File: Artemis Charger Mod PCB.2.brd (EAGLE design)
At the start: 95.9 x 94.6 mm, 159 parts, among them J1 MOLEX_CLICKMATE-2-VERTICAL, J2 MOLEX_CLICKMATE-4-VERTICAL, J3 MOLEX_CLICKMATE-2-VERTICAL, J4 MOLEX_CLICKMATE-2-VERTICAL, J5 MOLEX_CLICKMATE-2-VERTICAL, Q10 BSS138, Q11 BSS138, Q8 BSS138, Q9 BSS138, U10 TPS562219, U11 ISO7340, U12 ISO7340, U13 TPS562219, U14 MCP2515-TSSOP, U15 MCP2562, U17 CD4050BD, U18 CD4043B, U19 SN74LVC08ASOIC, U20 SN74LVC32ASOIC, U22 LTC1155, U23 CSD17506Q5A, U26 CSD17506Q5A, U27 LTC1155, U28 CSD17506Q5A, U29 LTC1155, U3 MAX5812, U30 CSD17506Q5A, U32 CSD17506Q5A, U34 CSD17506Q5A, U49 TL7712A-SOIC, U8 MAX5812, U9 TPS562219

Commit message: Fixed LED Silkscreens
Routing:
- net SI_SPI: track 95.7 -> 106.7 mm
- net SO_SPI: track 92.0 -> 97.7 mm
- net CS_SPI: track 52.6 -> 56.5 mm
- net SCK_SPI: track 103.5 -> 106.1 mm
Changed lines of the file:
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@@
 <wire x1="95.25" y1="-14.605" x2="-0.635" y2="-14.605" width="0" layer="20"/>
 <wire x1="-0.635" y1="-14.605" x2="-0.635" y2="80.01" width="0" layer="20"/>
-<wire x1="63.5" y1="69.85" x2="69.85" y2="69.85" width="0.254" layer="21"/>
-<wire x1="69.85" y1="69.85" x2="69.85" y2="65.405" width="0.254" layer="21"/>
-<wire x1="69.85" y1="65.405" x2="67.945" y2="65.405" width="0.254" layer="21"/>
-<wire x1="67.945" y1="65.405" x2="63.5" y2="65.405" width="0.254" layer="21"/>
-<wire x1="63.5" y1="65.405" x2="63.5" y2="69.85" width="0.254" layer="21"/>
+<wire x1="67.056" y1="70.358" x2="70.866" y2="70.358" width="0.254" layer="21"/>
+<wire x1="70.866" y1="70.358" x2="70.866" y2="65.151" width="0.254" layer="21"/>
+<wire x1="70.866" y1="65.151" x2="67.945" y2="65.151" width="0.254" layer="21"/>
+<wire x1="67.945" y1="65.151" x2="67.056" y2="65.151" width="0.254" layer="21"/>
+<wire x1="67.056" y1="65.151" x2="67.056" y2="70.358" width="0.254" layer="21"/>
 <wire x1="66.04" y1="56.515" x2="66.04" y2="55.88" width="0.254" layer="21"/>
 <wire x1="66.04" y1="55.88" x2="66.04" y2="52.705" width="0.254" layer="21"/>
@@
 <wire x1="66.04" y1="44.45" x2="66.04" y2="52.705" width="0.254" layer="21"/>
 <wire x1="84.455" y1="44.45" x2="66.04" y2="44.45" width="0.254" layer="21"/>
-<wire x1="67.945" y1="65.405" x2="67.945" y2="55.88" width="0.254" layer="21"/>
+<wire x1="67.945" y1="65.151" x2="67.945" y2="55.88" width="0.254" layer="21"/>
 <wire x1="67.945" y1="55.88" x2="66.04" y2="55.88" width="0.254" layer="21"/>
 <text x="40.64" y="-3.175" size="0.762" layer="21">Power Brick</text>
@@
 <attribute name="MF" value="" x="48.26" y="74.93" size="1.778" layer="27" display="off"/>
 <attribute name="PARTNO" value="598-8170-107F" x="48.26" y="74.93" size="1.778" layer="27" display="off"/>
-<attribute name="NAME" x="64.135" y="66.04" size="1.27" layer="25" font="vector"/>
+<attribute name="NAME" x="70.358" y="64.389" size="1.27" layer="25" font="vector" rot="R90"/>
 <attribute name="VALUE" x="67.31" y="53.34" size="1.27" layer="27" rot="R90"/>
 </element>
@@
 <attribute name="MF" value="" x="34.29" y="74.93" size="1.778" layer="27" display="off"/>
 <attribute name="PARTNO" value="598-8170-107F" x="34.29" y="74.93" size="1.778" layer="27" display="off"/>
-<attribute name="NAME" x="64.135" y="67.945" size="1.27" layer="25" font="vector"/>
+<attribute name="NAME" x="68.707" y="64.389" size="1.27" layer="25" font="vector" rot="R90"/>
 <attribute name="VALUE" x="64.77" y="53.34" size="1.27" layer="27" rot="R90"/>
 </element>
@@
 <contactref element="U14" pad="14"/>
 <contactref element="TP19" pad="TP"/>
-<wire x1="66.380003125" y1="59.984996875" x2="63.77899375" y2="59.984996875" width="0" layer="19" extent="1-1"/>
 <wire x1="69.215" y1="52.705" x2="68.58" y2="52.705" width="0" layer="19" extent="1-1"/>
+<wire x1="66.380003125" y1="59.984996875" x2="63.77899375" y2="59.984996875" width="0.4064" layer="1"/>
 </signal>
 <signal name="N$68">
@@
 <wire x1="71.755" y1="60.325" x2="71.755" y2="65.405" width="0.4064" layer="1"/>
 <wire x1="71.755" y1="65.405" x2="70.485" y2="65.405" width="0.4064" layer="1"/>
-<wire x1="70.485" y1="65.405" x2="68.8975" y2="66.9925" width="0.4064" layer="1"/>
+<wire x1="70.485" y1="65.405" x2="67.945" y2="67.945" width="0.4064" layer="1"/>
 <contactref element="JP1" pad="21"/>
-<wire x1="68.8975" y1="66.9925" x2="68.58" y2="67.31" width="0.4064" layer="1"/>
 <wire x1="67.31" y1="78.105" x2="67.31" y2="74.295" width="0.4064" layer="1"/>
 <wire x1="55.245" y1="67.31" x2="51.435" y2="63.5" width="0.4064" layer="1"/>
@@
 <wire x1="56.515" y1="67.31" x2="57.15" y2="67.945" width="0.4064" layer="1"/>
 <wire x1="57.15" y1="67.945" x2="67.945" y2="67.945" width="0.4064" layer="1"/>
-<wire x1="67.945" y1="67.945" x2="68.58" y2="67.31" width="0.4064" layer="1"/>
 <contactref element="U14" pad="17"/>
 <contactref element="TP12" pad="TP"/>
-<wire x1="68.874996875" y1="61.935003125" x2="63.77899375" y2="61.935003125" width="0" layer="19" extent="1-1"/>
-<wire x1="70.485" y1="57.15" x2="70.485" y2="57.785" width="0" layer="19" extent="1-1"/>
+<wire x1="68.874996875" y1="61.935003125" x2="63.77899375" y2="61.935003125" width="0.4064" layer="1"/>
+<wire x1="70.485" y1="57.15" x2="70.485" y2="57.785" width="0.4064" layer="1"/>
 </signal>
 <signal name="CS_SPI">
@@
 <contactref element="U14" pad="18"/>
 <contactref element="TP4" pad="TP"/>
-<wire x1="68.58" y1="59.055" x2="69.215" y2="59.055" width="0" layer="19" extent="1-1"/>
-<wire x1="63.77899375" y1="62.584990625" x2="67.029990625" y2="62.584990625" width="0" layer="19" extent="1-1"/>
+<wire x1="67.029990625" y1="62.584990625" x2="63.77899375" y2="62.584990625" width="0.4064" layer="1"/>
+<wire x1="69.215" y1="59.055" x2="68.58" y2="59.055" width="0.4064" layer="1"/>
 </signal>
 <signal name="N$77">
@@
 <via x="81.915" y="64.77" extent="1-16" drill="0.6"/>
 <wire x1="77.47" y1="64.135" x2="74.93" y2="66.675" width="0.4064" layer="16"/>
-<wire x1="74.93" y1="66.675" x2="70.485" y2="66.675" width="0.4064" layer="16"/>
-<via x="70.485" y="66.675" extent="1-16" drill="0.6"/>
-<wire x1="70.485" y1="66.675" x2="68.58" y2="68.58" width="0.4064" layer="1"/>
+<wire x1="74.93" y1="66.675" x2="71.755" y2="66.675" width="0.4064" layer="16"/>
+<via x="71.755" y="66.675" extent="1-16" drill="0.6"/>
 <via x="52.07" y="66.675" extent="1-16" drill="0.6"/>
 <via x="43.815" y="66.675" extent="1-16" drill="0.6"/>
@@
 <wire x1="53.34" y1="67.945" x2="55.88" y2="67.945" width="0.4064" layer="1"/>
 <wire x1="55.88" y1="67.945" x2="56.515" y2="68.58" width="0.4064" layer="1"/>
-<wire x1="56.515" y1="68.58" x2="68.58" y2="68.58" width="0.4064" layer="1"/>
+<wire x1="56.515" y1="68.58" x2="68.834" y2="68.58" width="0.4064" layer="1"/>
+<wire x1="68.834" y1="68.58" x2="70.866" y2="66.548" width="0.4064" layer="1"/>
+<wire x1="70.866" y1="66.548" x2="71.628" y2="66.548" width="0.4064" layer="1"/>
+<wire x1="71.628" y1="66.548" x2="71.755" y2="66.675" width="0.4064" layer="1"/>
 </signal>
 <signal name="AMS15V">
@@
 <contactref element="U14" pad="16"/>
 <contactref element="TP15" pad="TP"/>
-<wire x1="70.485" y1="61.595" x2="63.77899375" y2="61.28499375" width="0" layer="19" extent="1-16"/>
-<wire x1="70.485" y1="54.61" x2="71.12" y2="54.61" width="0" layer="19" extent="1-1"/>
+<wire x1="63.77899375" y1="61.28499375" x2="66.47700625" y2="61.28499375" width="0.4064" layer="1"/>
+<wire x1="66.47700625" y1="61.28499375" x2="67.818" y2="59.944" width="0.4064" layer="1"/>
+<wire x1="67.818" y1="59.944" x2="67.818" y2="57.658" width="0.4064" layer="1"/>
+<wire x1="67.818" y1="57.658" x2="70.358" y2="55.118" width="0.4064" layer="1"/>
+<wire x1="70.358" y1="55.118" x2="70.358" y2="54.737" width="0.4064" layer="1"/>
+<wire x1="70.358" y1="54.737" x2="70.485" y2="54.61" width="0.4064" layer="1"/>
+<wire x1="71.12" y1="54.61" x2="70.485" y2="54.61" width="0" layer="19" extent="1-1"/>
 </signal>
 <signal name="N$3">

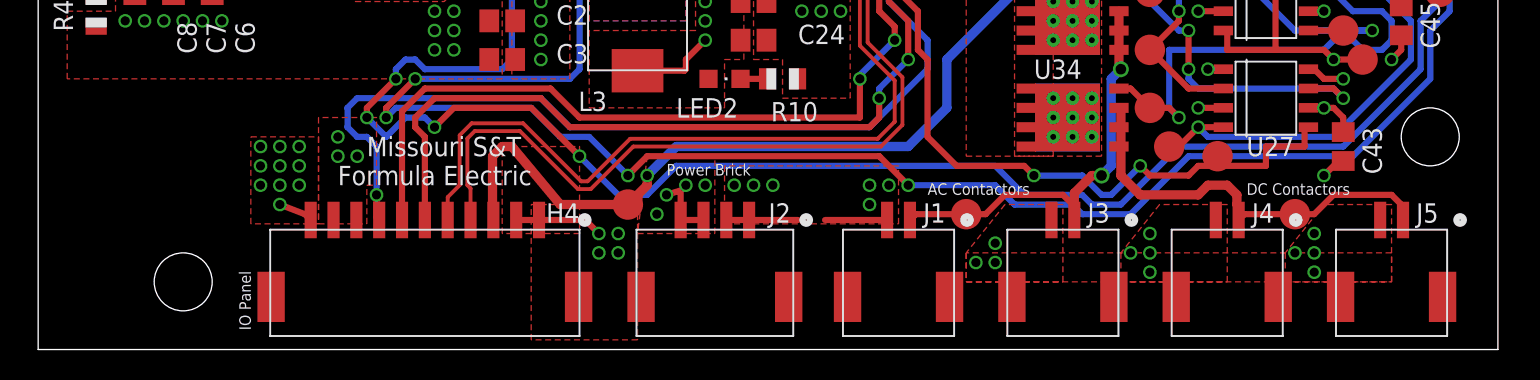
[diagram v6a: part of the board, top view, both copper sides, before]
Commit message: Added extra contactor for charger discharge
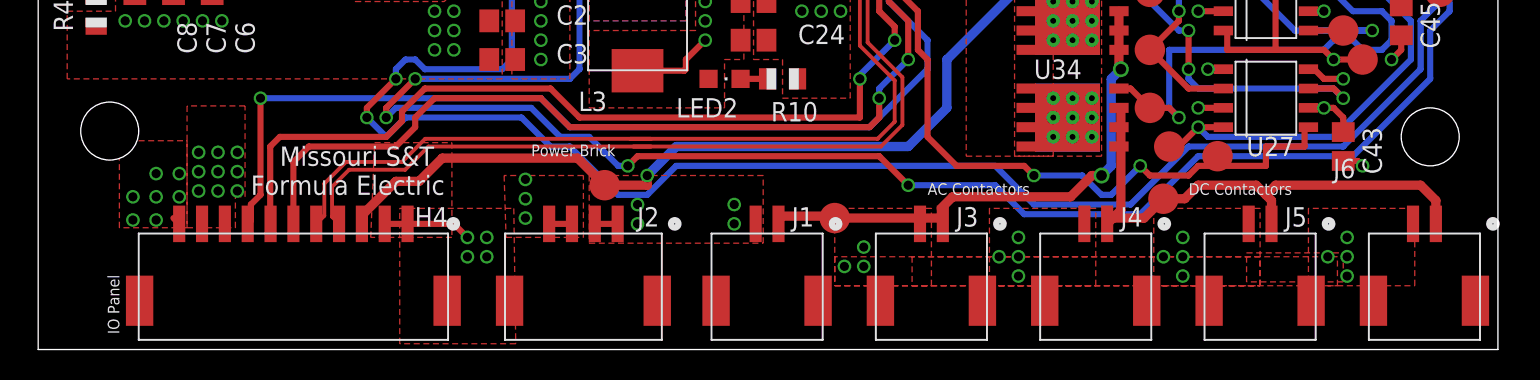
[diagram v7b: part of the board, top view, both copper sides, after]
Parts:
- added J6: MOLEX_CLICKMATE-2-VERTICAL, FormE:MOLEX-CLIKMATE-2-VERTICAL-HEADER
- moved TP16 8.70 mm to (73.3, -4.70)
- moved J1 8.64 mm to (47.2, -10.4)
- moved TP9 8.64 mm to (51.7, -5.97)
- moved H4 8.64 mm to (16.1, -10.4)
- moved J2 8.64 mm to (35.2, -10.4)
- moved J3 8.64 mm to (58.0, -10.4)
- moved J4 8.64 mm to (68.8, -10.4)
- moved J5 8.64 mm to (79.6, -10.4)
- moved TP8 1.98 mm to (36.6, -3.81)
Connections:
- net GND1: now also J6.2
- net N$6: now also J6.1
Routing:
- net N$6: track 27.8 -> 36.0 mm
- net IMD15V: track 84.7 -> 92.6 mm
- net GND1: track 200.5 -> 193.3 mm, vias 87 -> 95
- net RTDS_SOURCE1: track 28.3 -> 35.2 mm
- net AMS15V: track 72.6 -> 79.3 mm
- net INTERUPT15V: track 74.9 -> 80.6 mm
- net CAN_N: track 94.5 -> 99.9 mm
- net CAN_P: track 95.3 -> 100.7 mm
- net ACUMULATOR_CONTACTOR_SIGNAL: track 61.0 -> 65.8 mm
- net VDD: track 130.7 -> 127.8 mm, vias 33 -> 32
- net +3V3: track 237.3 -> 235.6 mm, vias 40 -> 37
- net SDA1_I2C: track 254.9 -> 253.8 mm, vias 10 -> 8
- net SCL1_I2C: track 250.2 -> 249.7 mm
- added copper zone on layer 1, net N$5

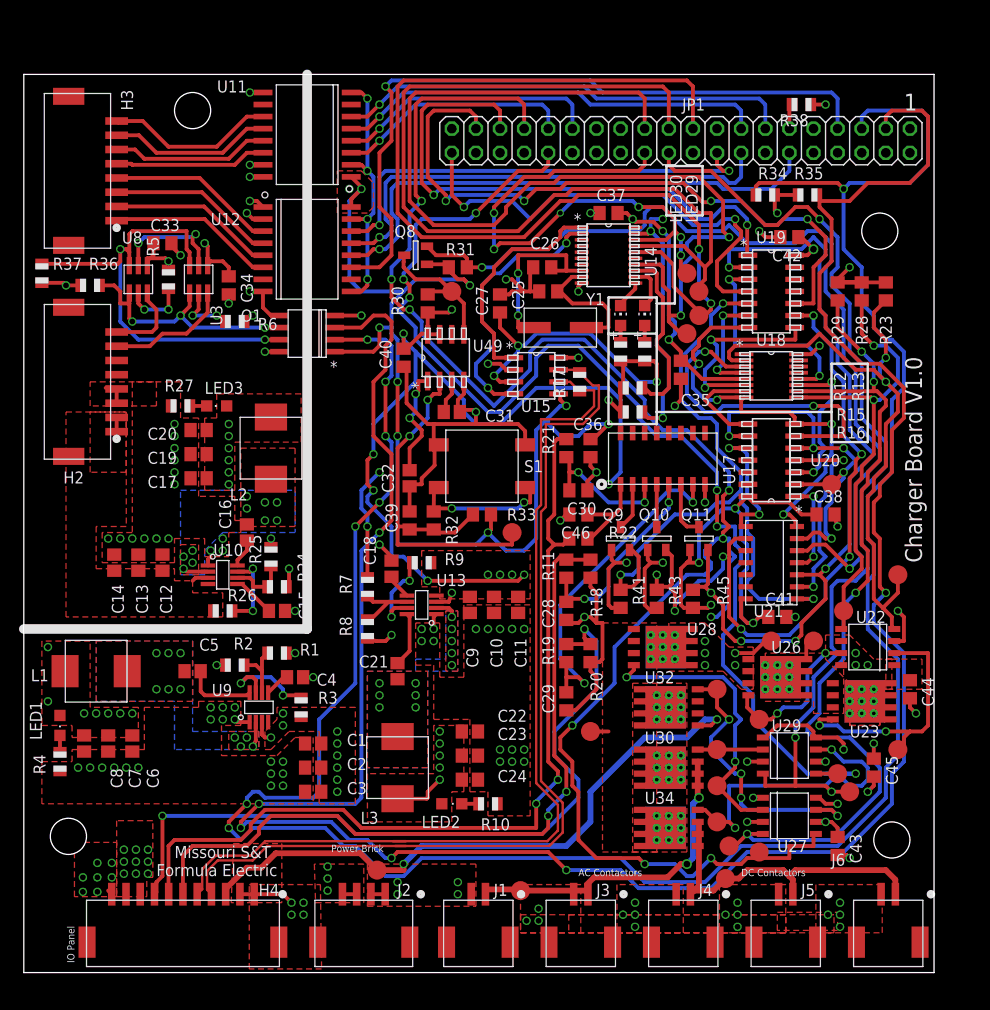
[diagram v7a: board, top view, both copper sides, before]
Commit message: Fixed fixed silk screens, fixed a few overlap errors
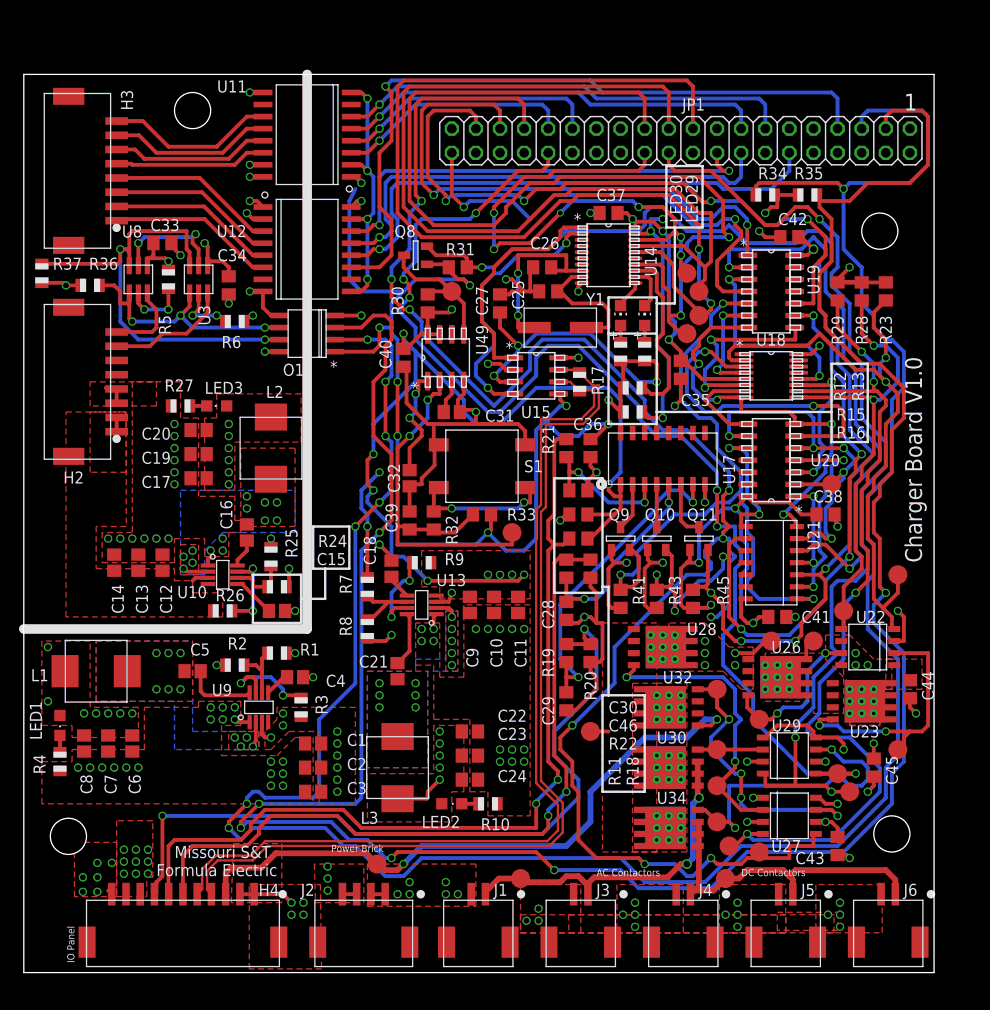
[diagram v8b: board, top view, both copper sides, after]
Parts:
- removed R38: 10K, adafruit:R0805
- moved TP9 1.27 mm to (51.7, -4.70)
- moved TP8 0.64 mm to (36.6, -3.17)
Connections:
- removed net N$3: JP1.11, R38.2
- net GND1: no longer R38.1
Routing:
- net N$3: track 2.65 -> 0.00 mm
- net VDD: track 127.8 -> 129.9 mm
- net N$50: track 36.4 -> 34.6 mm
- net GND1: track 193.3 -> 191.7 mm, vias 95 -> 96
- net BSPD_FET_SIGNAL3: track 126.2 -> 124.9 mm
- net CAN_N: track 99.9 -> 98.6 mm
- net CAN_P: track 100.7 -> 99.6 mm
- net ACUMULATOR_CONTACTOR_SIGNAL: track 65.8 -> 66.9 mm
- net RTDS_SOURCE1: track 35.2 -> 36.3 mm
- net SI_SPI: track 106.7 -> 107.4 mm
- net SCK_SPI: track 106.1 -> 106.7 mm
- net BSPD_FET_SIGNAL2: track 100.5 -> 101.0 mm
- net BSPD_FET_SIGNAL1: track 178.6 -> 179.1 mm
- net +3V3: track 235.6 -> 235.3 mm, vias 37 -> 36
- removed copper zone on layer 1, net N$5
